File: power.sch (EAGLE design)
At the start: 114 parts, among them Q1 IXTK180N15P, Q2 IXTK180N15P, Q3 2N7002, Q4 SPD15P10PL, Q5 2N7002, U1 LT1630, U10 LM2936, U11 LM317, U2 LT1630, U3 DCDC 15V, U4 DAC80501, U5 DAC80501, U6 ADS1120, U7 LM2662, U8 LM7805, U9 TPS3700

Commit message: Progress on PCBs
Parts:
- added CN1: 0530471210, CONNECTORs:PICOBLADE_12_TH_V
- added D8: 12V BI TVS, DIODES:SMBJ12CA-13-F
- added MECH10, MECH11, MECH12, MECH13: 6mm x 3mm, MISC:MOUNTHOLE
- added TP1, TP2, TP3, TP4: TEST_POINT_SQUARE, MISC:TEST_POINT_SQUARE
- C27, C29, C34, C40, C44, C46, C7: value 100nF 16V -> 100nF 100V; device CAPACITORS:CL10B104KO8WPNC -> CAPACITORS:06031C104KAT2A
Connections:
- net 3V3D: now also CN1.3, CN1.4
- net ADC_!DRDY: now also CN1.7
- net ADC_SPI_!CS: now also CN1.8
- net ADC_SPI_MISO: now also CN1.6
- net ADC_SPI_MOSI: now also CN1.5
- net ADC_SPI_SCLK: now also CN1.9
- net AGND: no longer C44.1, C45.1, U10.GND
- net DAC_I2C_SCL: now also CN1.1
- net DAC_I2C_SDA: now also CN1.2
- net DGND: now also CN1.10, CN1.11, CN1.12, U6.CLK
- net N$12: now also RL1C.1; no longer RL1B.1
- net N$14: now also RL1B.1; no longer RL1C.1
- net N$26: now also TP4.P$1
- net N$27: now also TP3.P$1
- net PGND: now also C44.1, C45.1, U10.GND
- net VOUT+: now also D8.K, RL1C.3, TP1.P$1; no longer RL1B.3
- net VOUT-: now also D8.A, RL1B.3, TP2.P$1; no longer RL1C.3
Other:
- moved on the sheet: RL1B, RL1C

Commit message: Progress
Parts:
- added MECH14, MECH15: 6mm x 3mm, MISC:MOUNTHOLE
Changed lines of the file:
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@@
 <part name="TP3" library="MISC" deviceset="TEST_POINT_SQUARE" device=""/>
 <part name="TP4" library="MISC" deviceset="TEST_POINT_SQUARE" device=""/>
+<part name="MECH14" library="MISC" deviceset="MOUNTHOLE" device="" value="6mm x 3mm"/>
+<part name="MECH15" library="MISC" deviceset="MOUNTHOLE" device="" value="6mm x 3mm"/>
 </parts>
 <sheets>
@@
 <attribute name="NAME" x="25.4" y="457.2" size="1.27" layer="97" rot="R90" align="center"/>
 </instance>
+<instance part="MECH14" gate="G$1" x="383.54" y="386.08" smashed="yes">
+<attribute name="NAME" x="383.54" y="389.636" size="1.27" layer="95" align="center"/>
+</instance>
+<instance part="MECH15" gate="G$1" x="391.16" y="386.08" smashed="yes">
+<attribute name="NAME" x="391.16" y="389.636" size="1.27" layer="95" align="center"/>
+</instance>
 </instances>

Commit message: Control nearly done
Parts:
- removed CN1: 0530471210, CONNECTORs:PICOBLADE_12_TH_V
- added CN2: 2X10 HEADER, CONNECTORs:2X10_HEADER
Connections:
- removed net N$36: Q4.D, U3.VIN+
- new net VOUT: CN2.13, CN2.14, CN2.7, CN2.8, Q4.D, U3.VIN+
- net 3V3D: now also CN2.19, CN2.2; no longer CN1.3, CN1.4
- net ADC_!DRDY: now also CN2.5; no longer CN1.7
- net ADC_SPI_!CS: now also CN2.15; no longer CN1.8
- net ADC_SPI_MISO: now also CN2.4; no longer CN1.6
- net ADC_SPI_MOSI: now also CN2.3; no longer CN1.5
- net ADC_SPI_SCLK: now also CN2.6; no longer CN1.9
- net DAC_I2C_SCL: now also CN2.17; no longer CN1.1
- net DAC_I2C_SDA: now also CN2.18; no longer CN1.2
- net DGND: now also CN2.1, CN2.16, CN2.20; no longer CN1.10, CN1.11, CN1.12
- net PGND: now also CN2.10, CN2.11, CN2.12, CN2.9
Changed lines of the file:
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@@
 <part name="MECH12" library="MISC" deviceset="MOUNTHOLE" device="" value="6mm x 3mm"/>
 <part name="MECH13" library="MISC" deviceset="MOUNTHOLE" device="" value="6mm x 3mm"/>
-<part name="CN1" library="CONNECTORs" deviceset="PICOBLADE_12_" device="TH_V" value="0530471210"/>
 <part name="TP3" library="MISC" deviceset="TEST_POINT_SQUARE" device=""/>
 <part name="TP4" library="MISC" deviceset="TEST_POINT_SQUARE" device=""/>
 <part name="MECH14" library="MISC" deviceset="MOUNTHOLE" device="" value="6mm x 3mm"/>
 <part name="MECH15" library="MISC" deviceset="MOUNTHOLE" device="" value="6mm x 3mm"/>
+<part name="CN2" library="CONNECTORs" deviceset="2X10_HEADER" device="" value="2X10 HEADER"/>
+<part name="U$80" library="NETS" deviceset="VOUT" device=""/>
 </parts>
 <sheets>
@@
 <attribute name="NAME" x="391.16" y="407.416" size="1.27" layer="95" align="center"/>
 </instance>
-<instance part="CN1" gate="G$1" x="261.62" y="287.02" smashed="yes">
-<attribute name="NAME" x="256.54" y="307.34" size="2.286" layer="95"/>
-<attribute name="VALUE" x="256.54" y="304.8" size="2.286" layer="96"/>
-</instance>
 <instance part="TP3" gate="G$1" x="27.94" y="452.12" smashed="yes" rot="R90">
 <attribute name="NAME" x="25.4" y="452.12" size="1.27" layer="97" rot="R90" align="center"/>
@@
 <instance part="MECH15" gate="G$1" x="391.16" y="386.08" smashed="yes">
 <attribute name="NAME" x="391.16" y="389.636" size="1.27" layer="95" align="center"/>
+</instance>
+<instance part="CN2" gate="G$1" x="2.54" y="264.16" smashed="yes">
+<attribute name="NAME" x="-2.54" y="281.94" size="1.27" layer="95"/>
+<attribute name="VALUE" x="-2.54" y="279.4" size="1.27" layer="96"/>
+</instance>
+<instance part="U$80" gate="G$1" x="137.16" y="474.98" smashed="yes">
+<attribute name="VALUE" x="137.16" y="477.52" size="1.778" layer="96" rot="R180" align="center"/>
 </instance>
 </instances>
@@
 </segment>
 <segment>
-<pinref part="CN1" gate="G$1" pin="1"/>
-<wire x1="269.24" y1="299.72" x2="302.26" y2="299.72" width="0.1524" layer="91"/>
-<label x="271.78" y="299.72" size="1.778" layer="95"/>
+<pinref part="CN2" gate="G$1" pin="17"/>
+<wire x1="12.7" y1="266.7" x2="40.64" y2="266.7" width="0.1524" layer="91"/>
+<label x="15.24" y="266.7" size="1.778" layer="95"/>
 </segment>
 </net>
@@
 </segment>
 <segment>
-<pinref part="CN1" gate="G$1" pin="2"/>
-<wire x1="269.24" y1="297.18" x2="302.26" y2="297.18" width="0.1524" layer="91"/>
-<label x="271.78" y="297.18" size="1.778" layer="95"/>
+<pinref part="CN2" gate="G$1" pin="18"/>
+<wire x1="12.7" y1="269.24" x2="40.64" y2="269.24" width="0.1524" layer="91"/>
+<label x="15.24" y="269.24" size="1.778" layer="95"/>
 </segment>
 </net>
@@
 </segment>
 <segment>
-<pinref part="CN1" gate="G$1" pin="10"/>
-<wire x1="269.24" y1="276.86" x2="302.26" y2="276.86" width="0.1524" layer="91"/>
-<label x="271.78" y="276.86" size="1.778" layer="95"/>
-</segment>
-<segment>
-<pinref part="CN1" gate="G$1" pin="11"/>
-<wire x1="269.24" y1="274.32" x2="302.26" y2="274.32" width="0.1524" layer="91"/>
-<label x="271.78" y="274.32" size="1.778" layer="95"/>
-</segment>
-<segment>
-<pinref part="CN1" gate="G$1" pin="12"/>
-<wire x1="269.24" y1="271.78" x2="302.26" y2="271.78" width="0.1524" layer="91"/>
-<label x="271.78" y="271.78" size="1.778" layer="95"/>
-</segment>
-<segment>
 <pinref part="U6" gate="G$1" pin="CLK"/>
 <wire x1="200.66" y1="261.62" x2="231.14" y2="261.62" width="0.1524" layer="91"/>
 <label x="205.74" y="261.62" size="1.778" layer="95"/>
+</segment>
+<segment>
+<pinref part="CN2" gate="G$1" pin="1"/>
+<wire x1="-7.62" y1="274.32" x2="-35.56" y2="274.32" width="0.1524" layer="91"/>
+<label x="-33.02" y="274.32" size="1.778" layer="95"/>
+</segment>
+<segment>
+<pinref part="CN2" gate="G$1" pin="20"/>
+<wire x1="12.7" y1="274.32" x2="40.64" y2="274.32" width="0.1524" layer="91"/>
+<label x="15.24" y="274.32" size="1.778" layer="95"/>
+</segment>
+<segment>
+<pinref part="CN2" gate="G$1" pin="16"/>
+<wire x1="12.7" y1="264.16" x2="40.64" y2="264.16" width="0.1524" layer="91"/>
+<label x="15.24" y="264.16" size="1.778" layer="95"/>
 </segment>
 </net>
@@
 </segment>
 <segment>
-<pinref part="CN1" gate="G$1" pin="3"/>
-<wire x1="269.24" y1="294.64" x2="302.26" y2="294.64" width="0.1524" layer="91"/>
-<label x="271.78" y="294.64" size="1.778" layer="95"/>
-</segment>
-<segment>
-<pinref part="CN1" gate="G$1" pin="4"/>
-<wire x1="269.24" y1="292.1" x2="302.26" y2="292.1" width="0.1524" layer="91"/>
-<label x="271.78" y="292.1" size="1.778" layer="95"/>
+<pinref part="CN2" gate="G$1" pin="2"/>
+<wire x1="-7.62" y1="271.78" x2="-35.56" y2="271.78" width="0.1524" layer="91"/>
+<label x="-33.02" y="271.78" size="1.778" layer="95"/>
+</segment>
+<segment>
+<pinref part="CN2" gate="G$1" pin="19"/>
+<wire x1="12.7" y1="271.78" x2="40.64" y2="271.78" width="0.1524" layer="91"/>
+<label x="15.24" y="271.78" size="1.778" layer="95"/>
 </segment>
 </net>
@@
 </segment>
 <segment>
-<pinref part="CN1" gate="G$1" pin="8"/>
-<wire x1="269.24" y1="281.94" x2="302.26" y2="281.94" width="0.1524" layer="91"/>
-<label x="271.78" y="281.94" size="1.778" layer="95"/>
+<pinref part="CN2" gate="G$1" pin="15"/>
+<wire x1="12.7" y1="261.62" x2="40.64" y2="261.62" width="0.1524" layer="91"/>
+<label x="15.24" y="261.62" size="1.778" layer="95"/>
 </segment>
 </net>
@@
 </segment>
 <segment>
-<pinref part="CN1" gate="G$1" pin="9"/>
-<wire x1="269.24" y1="279.4" x2="302.26" y2="279.4" width="0.1524" layer="91"/>
-<label x="271.78" y="279.4" size="1.778" layer="95"/>
+<pinref part="CN2" gate="G$1" pin="6"/>
+<wire x1="-7.62" y1="261.62" x2="-35.56" y2="261.62" width="0.1524" layer="91"/>
+<label x="-33.02" y="261.62" size="1.778" layer="95"/>
 </segment>
 </net>
@@
 </segment>
 <segment>
-<pinref part="CN1" gate="G$1" pin="5"/>
-<wire x1="269.24" y1="289.56" x2="302.26" y2="289.56" width="0.1524" layer="91"/>
-<label x="271.78" y="289.56" size="1.778" layer="95"/>
+<pinref part="CN2" gate="G$1" pin="3"/>
+<wire x1="-7.62" y1="269.24" x2="-35.56" y2="269.24" width="0.1524" layer="91"/>
+<label x="-33.02" y="269.24" size="1.778" layer="95"/>
 </segment>
 </net>
@@
 </segment>
 <segment>
-<pinref part="CN1" gate="G$1" pin="6"/>
-<wire x1="269.24" y1="287.02" x2="302.26" y2="287.02" width="0.1524" layer="91"/>
-<label x="271.78" y="287.02" size="1.778" layer="95"/>
+<pinref part="CN2" gate="G$1" pin="4"/>
+<wire x1="-7.62" y1="266.7" x2="-35.56" y2="266.7" width="0.1524" layer="91"/>
+<label x="-33.02" y="266.7" size="1.778" layer="95"/>
 </segment>
 </net>
@@
 </segment>
 <segment>
-<pinref part="CN1" gate="G$1" pin="7"/>
-<wire x1="269.24" y1="284.48" x2="302.26" y2="284.48" width="0.1524" layer="91"/>
-<label x="271.78" y="284.48" size="1.778" layer="95"/>
+<pinref part="CN2" gate="G$1" pin="5"/>
+<wire x1="-7.62" y1="264.16" x2="-35.56" y2="264.16" width="0.1524" layer="91"/>
+<label x="-33.02" y="264.16" size="1.778" layer="95"/>
 </segment>
 </net>
@@
 <wire x1="68.58" y1="342.9" x2="68.58" y2="345.44" width="0.1524" layer="91"/>
 <junction x="68.58" y="345.44"/>
-</segment>
-</net>
-<net name="N$36" class="0">
-<segment>
-<pinref part="U3" gate="G$1" pin="VIN+"/>
-<wire x1="144.78" y1="469.9" x2="134.62" y2="469.9" width="0.1524" layer="91"/>
-<pinref part="Q4" gate="G$1" pin="D"/>
 </segment>
 </net>
@@
 <wire x1="50.8" y1="396.24" x2="50.8" y2="398.78" width="0.1524" layer="91"/>
 <pinref part="U$68" gate="G$1" pin="PGND"/>
+</segment>
+<segment>
+<pinref part="CN2" gate="G$1" pin="10"/>
+<wire x1="-7.62" y1="251.46" x2="-35.56" y2="251.46" width="0.1524" layer="91"/>
+<label x="-33.02" y="251.46" size="1.778" layer="95"/>
+</segment>
+<segment>
+<pinref part="CN2" gate="G$1" pin="11"/>
+<wire x1="12.7" y1="251.46" x2="40.64" y2="251.46" width="0.1524" layer="91"/>
+<label x="15.24" y="251.46" size="1.778" layer="95"/>
+</segment>
+<segment>
+<pinref part="CN2" gate="G$1" pin="12"/>
+<wire x1="12.7" y1="254" x2="40.64" y2="254" width="0.1524" layer="91"/>
+<label x="15.24" y="254" size="1.778" layer="95"/>
+</segment>
+<segment>
+<pinref part="CN2" gate="G$1" pin="9"/>
+<wire x1="-7.62" y1="254" x2="-35.56" y2="254" width="0.1524" layer="91"/>
+<label x="-33.02" y="254" size="1.778" layer="95"/>
 </segment>
 </net>
@@
 </segment>
 </net>
+<net name="VOUT" class="0">
+<segment>
+<pinref part="U3" gate="G$1" pin="VIN+"/>
+<wire x1="144.78" y1="469.9" x2="137.16" y2="469.9" width="0.1524" layer="91"/>
+<pinref part="Q4" gate="G$1" pin="D"/>
+<pinref part="U$80" gate="G$1" pin="VOUT"/>
+<wire x1="137.16" y1="469.9" x2="134.62" y2="469.9" width="0.1524" layer="91"/>
+<wire x1="137.16" y1="472.44" x2="137.16" y2="469.9" width="0.1524" layer="91"/>
+<junction x="137.16" y="469.9"/>
+</segment>
+<segment>
+<pinref part="CN2" gate="G$1" pin="8"/>
+<wire x1="-7.62" y1="256.54" x2="-35.56" y2="256.54" width="0.1524" layer="91"/>
+<label x="-33.02" y="256.54" size="1.778" layer="95"/>
+</segment>
+<segment>
+<pinref part="CN2" gate="G$1" pin="7"/>
+<wire x1="-7.62" y1="259.08" x2="-35.56" y2="259.08" width="0.1524" layer="91"/>
+<label x="-33.02" y="259.08" size="1.778" layer="95"/>
+</segment>
+<segment>
+<pinref part="CN2" gate="G$1" pin="13"/>
+<wire x1="12.7" y1="256.54" x2="40.64" y2="256.54" width="0.1524" layer="91"/>
+<label x="15.24" y="256.54" size="1.778" layer="95"/>
+</segment>
+<segment>
+<pinref part="CN2" gate="G$1" pin="14"/>
+<wire x1="12.7" y1="259.08" x2="40.64" y2="259.08" width="0.1524" layer="91"/>
+<label x="15.24" y="259.08" size="1.778" layer="95"/>
+</segment>
+</net>

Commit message: Female header added to the power PCB
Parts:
- CN2: device CONNECTORs:2X10_HEADER -> CONNECTORs:2X10_HEADER_FEMALE
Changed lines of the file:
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@@
 <part name="MECH14" library="MISC" deviceset="MOUNTHOLE" device="" value="6mm x 3mm"/>
 <part name="MECH15" library="MISC" deviceset="MOUNTHOLE" device="" value="6mm x 3mm"/>
-<part name="CN2" library="CONNECTORs" deviceset="2X10_HEADER" device="" value="2X10 HEADER"/>
+<part name="CN2" library="CONNECTORs" deviceset="2X10_HEADER_FEMALE" device="" value="2X10 HEADER"/>
 <part name="U$80" library="NETS" deviceset="VOUT" device=""/>
 </parts>

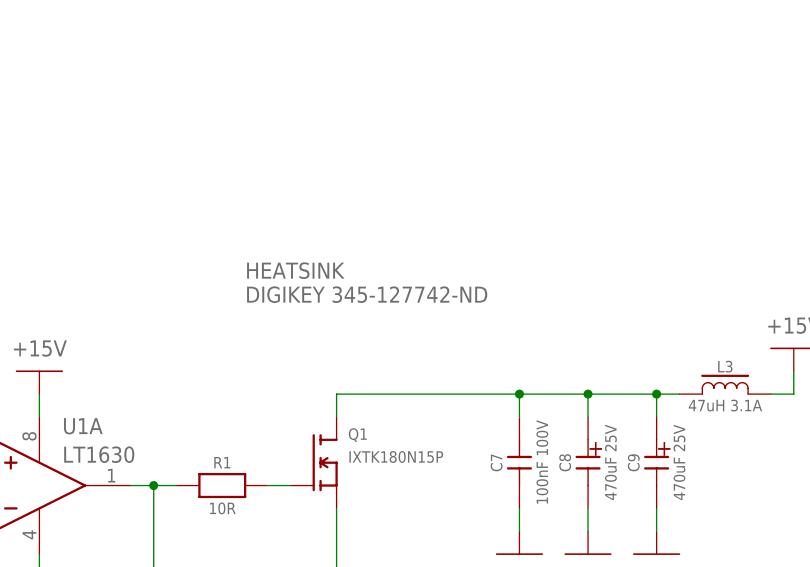
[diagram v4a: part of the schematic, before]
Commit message: BoM sorted for the power PCB
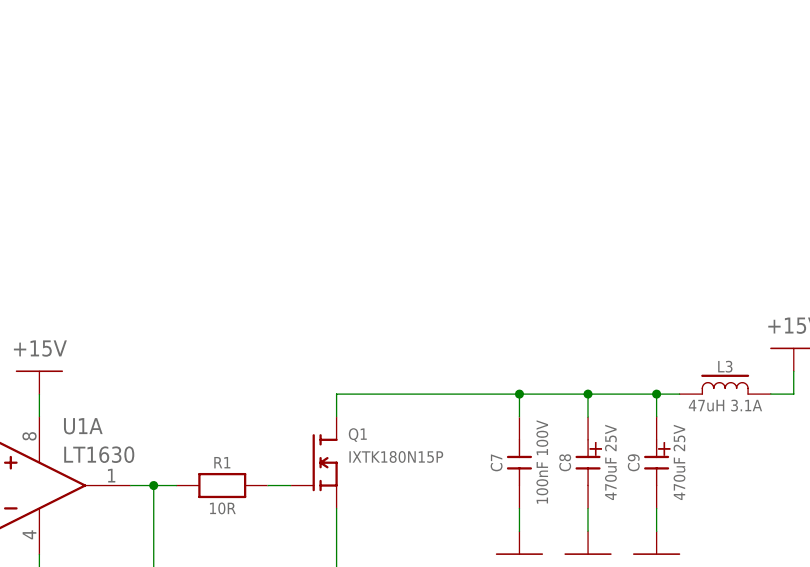
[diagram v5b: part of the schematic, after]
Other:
- note removed: "HEATSINK DIGIKEY 345-127742-ND"
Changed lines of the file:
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@@
 <text x="63.5" y="375.92" size="1.778" layer="94" rot="R180">OUTB = 0V WHEN VBAT &gt; 35V
 OUTA = 0V WHEN VBAT &lt; 9.2V</text>
-<text x="287.02" y="195.58" size="1.778" layer="95">HEATSINK
-DIGIKEY 345-127742-ND</text>
 </plain>
 <instances>
